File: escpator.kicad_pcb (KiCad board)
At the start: 4 copper layers, 45.7 x 15 mm, 36 parts, among them J1 Conn_01x04_Pin, J2 Conn_02x05_Odd_Even, J3 Conn_01x05, U1 STM32F103CBTx, U3 SRV05-4, U4 MCP1700x-330xxTT, X1 8MHz(12pF)

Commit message: second
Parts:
- removed X1: 8MHz(12pF), Crystal:Crystal_HC49-U_Vertical
- added Y1: Crystal_GND24, Crystal:Crystal_SMD_3225-4Pin_3.2x2.5mm_HandSoldering, F.Cu at (116.5, 36.9)
- C10, C14, C15, C3, C4, C5, C6, C7, C8, C9, R2, R3, R4, U3: moved to F.Cu
- C11, F1, R20, R27: moved to B.Cu
- moved C9 21.3 mm to (113.7, 33.0), turned to 0 degrees
- moved C10 17.7 mm to (109.4, 38.9), turned to 90 degrees
- moved C4 17.4 mm to (120.4, 32.1), turned to 180 degrees
- moved C3 15.5 mm to (108.4, 42.7), turned to -90 degrees
- moved R20 14.3 mm to (123.1, 40.5), turned to 90 degrees
- moved R1 13.5 mm to (123.5, 31.0)
- moved C5 12.9 mm to (120.4, 33.6), turned to 180 degrees
- moved R14 10.9 mm to (113.1, 38.8), turned to 135 degrees
- moved U4 10.7 mm to (133.2, 35.3), turned to -90 degrees
- moved C6 10.0 mm to (130.3, 33.0)
- moved C8 8.72 mm to (119.8, 40.4), turned to -90 degrees
- moved D1 5.74 mm to (111.3, 41.3), turned to 180 degrees
- moved R13 5.58 mm to (114.0, 31.3)
- moved R27 5.33 mm to (114.6, 42.3)
- moved D2 5.03 mm to (111.3, 42.8)
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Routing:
- net Earth: track 150.7 -> 195.2 mm, vias 13 -> 8
- net /AIN1: track 21.7 -> 4.45 mm, vias 2 -> 1
- net Net-(J2-Pin_3): track 20.5 -> 5.41 mm, vias 1 -> 0
- net /T_NRST: track 18.7 -> 3.91 mm
- net /T_JTMS: track 33.1 -> 20.7 mm, vias 4 -> 2
- net Net-(J2-Pin_2): track 25.6 -> 14.1 mm
- net /STLINK_TX: track 19.3 -> 26.6 mm
- net /LED_STLINK: track 14.7 -> 20.6 mm, vias 2 -> 1
- net Net-(J2-Pin_1): track 12.2 -> 17.9 mm, vias 1 -> 0
- net /T_JTCK: track 15.4 -> 20.5 mm
- net Net-(J1-Pin_1): track 12.8 -> 8.13 mm, vias 0 -> 1
- net /USB_P: track 11.5 -> 7.57 mm, vias 1 -> 0
- net +3V3: track 103.4 -> 99.5 mm, vias 7 -> 8
- net /OSC_OUT: track 10.8 -> 6.93 mm
- net /SWCLK: track 8.73 -> 5.13 mm
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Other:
- outline, holes or cut-outs redrawn

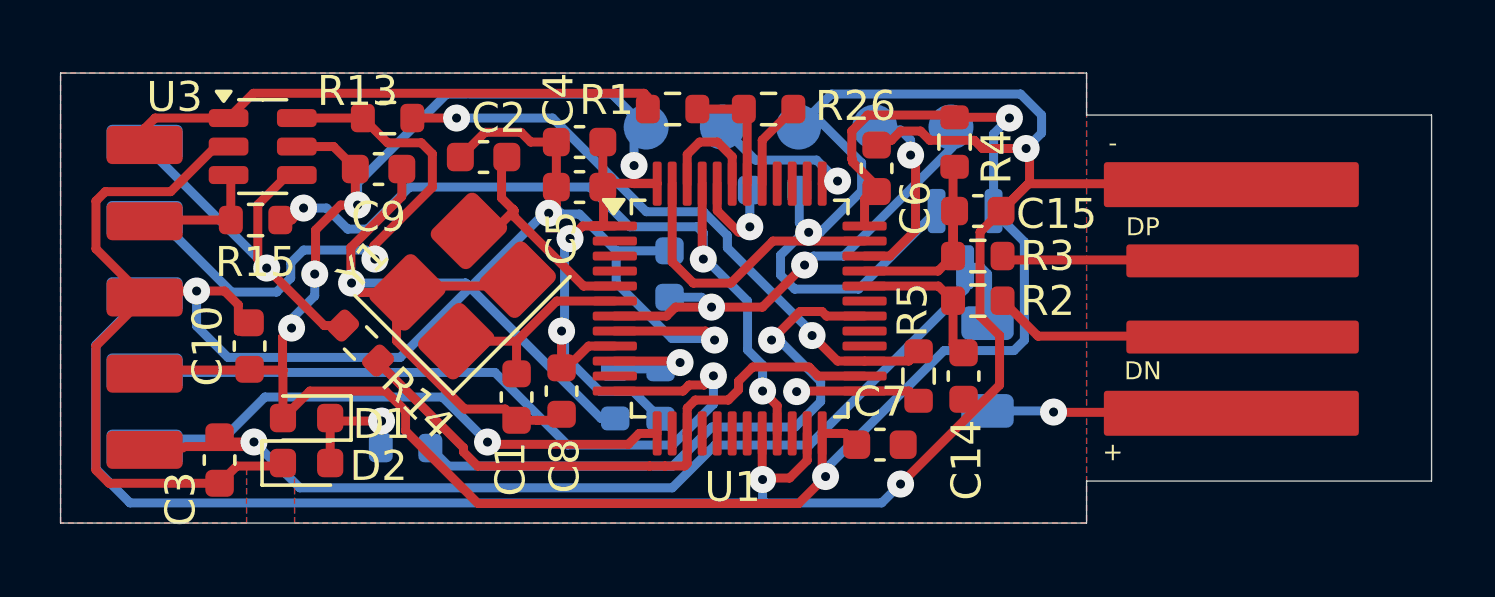
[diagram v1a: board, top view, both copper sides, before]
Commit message: presun LED plus otoceni USB
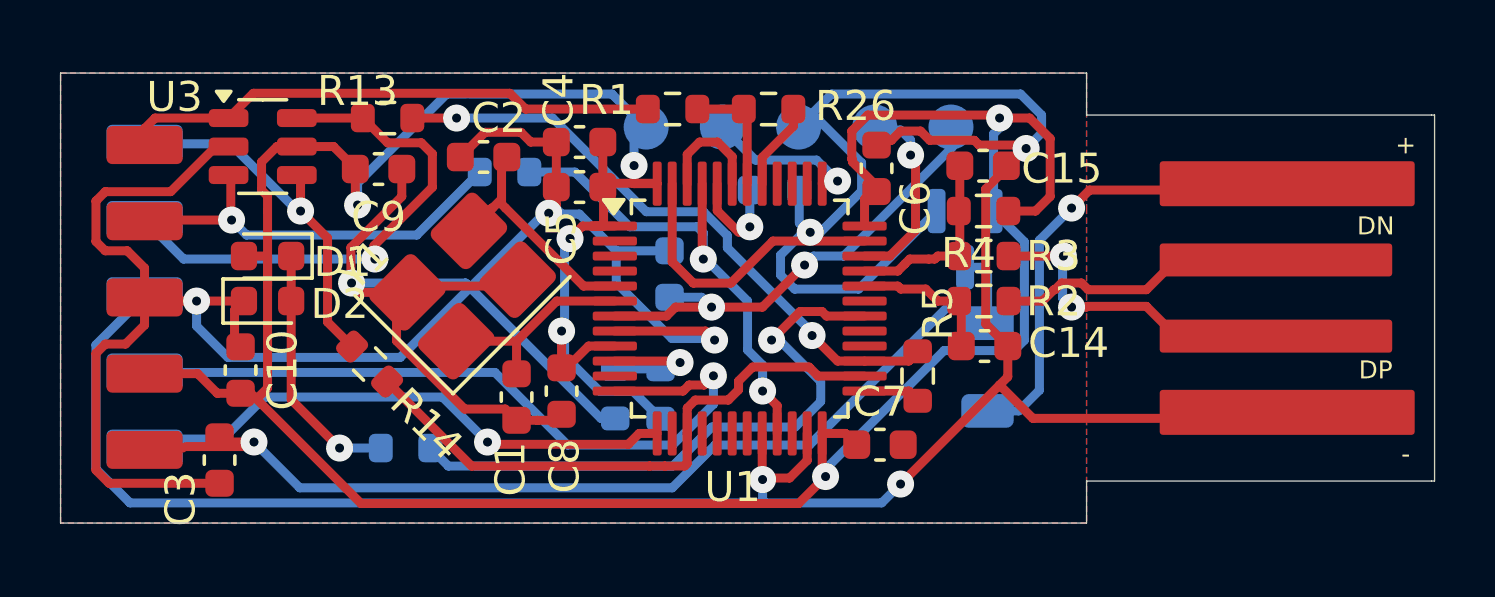
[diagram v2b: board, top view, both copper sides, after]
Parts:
- R15: moved to B.Cu
- moved J1 11.6 mm to (148.8, 37.3), turned to 180 degrees
- moved R15 8.45 mm to (117.9, 33.1)
- moved D1 5.55 mm to (110.0, 35.9)
- moved D2 5.55 mm to (110.0, 37.4)
- moved R4 2.49 mm to (133.9, 34.4), turned to 180 degrees
- moved C15 1.52 mm to (133.8, 32.9)
- moved C14 1.22 mm to (133.9, 38.9), turned to 0 degrees
- moved C10 0.85 mm to (109.1, 39.7)
- moved R14 0.76 mm to (113.4, 39.5)
- moved R2 0.20 mm to (133.9, 37.4)
- moved R3 0.20 mm to (133.9, 35.9)
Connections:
- net Net-(J1-Pin_2) renamed /D-
- net Net-(J1-Pin_3) renamed /D+
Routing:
- net Net-(J2-Pin_3): track 5.41 -> 14.8 mm, vias 0 -> 1
- net /T_SWIM: track 26.2 -> 17.1 mm, vias 3 -> 2
- net Net-(J1-Pin_1): track 8.13 -> 16.0 mm
- net +3V3: track 99.5 -> 106.1 mm, vias 8 -> 6
- net Net-(D1-K): track 4.48 -> 8.44 mm
- net /D+: track 8.04 -> 10.9 mm, vias 0 -> 2
- net /T_SWDIO_IN: track 4.41 -> 2.13 mm, vias 1 -> 0
- net /USB_P: track 7.57 -> 6.38 mm
- net /D-: track 8.48 -> 9.67 mm
- net Net-(J2-Pin_4): track 20.5 -> 19.4 mm
- net /T_JTCK: track 20.5 -> 19.8 mm
- net Net-(J2-Pin_2): track 14.1 -> 13.5 mm
- net /OSC_IN?: track 8.35 -> 8.90 mm
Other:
- board size 45.7 x 15 mm -> 45.8 x 15 mm

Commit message: changes
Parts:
- moved C3 1.10 mm to (109.5, 42.7)
- moved U4 0.90 mm to (134.2, 35.3)
- moved J3 0.88 mm to (126.7, 34.1)
- moved C6 0.81 mm to (129.8, 32.3)
- moved R26 0.48 mm to (126.5, 31.4)
- moved R1 0.27 mm to (123.5, 31.3)
- moved R7 0.07 mm to (126.8, 33.8)
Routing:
- net Earth: track 195.2 -> 181.7 mm
- net +3V3: track 106.1 -> 99.4 mm
- net +5V: track 36.1 -> 33.0 mm
- net /SWCLK: track 5.13 -> 7.12 mm
- net /T_SWIM: track 17.1 -> 15.9 mm
- net /SWDIO: track 6.55 -> 7.22 mm
- net /STM_RST: track 15.1 -> 15.7 mm
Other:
- board size 45.8 x 15 mm -> 45.7 x 15 mm
- board text added: "3V3"
- board text added: "5V"
- board text added: "STM_RST"
- board text added: "SWCLK"
- board text added: "SWDIO"
- board text added: "⏚"

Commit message: changedpins
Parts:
- removed U3: SRV05-4, Package_TO_SOT_SMD:SOT-23-6
- added R6: 100R, Resistor_SMD:R_0603_1608Metric, B.Cu at (32.2, 40.5)
- added R8: 100R, Resistor_SMD:R_0603_1608Metric, B.Cu at (30.7, 42.1)
- moved R14 79.7 mm to (33.7, 40.4)
- moved C7 78.7 mm to (51.7, 42.0)
- moved C1 78.7 mm to (39.6, 40.4)
- moved C11 78.7 mm to (44.7, 36.3)
- moved C14 78.7 mm to (55.2, 38.7)
- moved C15 78.7 mm to (55.2, 32.7)
- moved C2 78.7 mm to (38.5, 32.4)
- moved C3 78.7 mm to (30.8, 42.5)
- moved C4 78.7 mm to (41.7, 31.9)
- moved C5 78.7 mm to (41.7, 33.4)
- moved C6 78.7 mm to (51.2, 32.1)
- moved C8 78.7 mm to (41.1, 40.2)
- moved C9 78.7 mm to (35.0, 32.8)
- moved D1 78.7 mm to (31.3, 35.7)
- moved D2 78.7 mm to (31.3, 37.2)
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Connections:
- J2 pad 1: Net-(J2-Pin_1) -> +3V3
- J2 pad 10: /STLINK_RX -> Net-(J2-Pin_10)
- J2 pad 7: +3V3 -> Net-(J2-Pin_7)
- J2 pad 8: /STLINK_TX -> Net-(J2-Pin_8)
- R1 pad 1: Net-(J2-Pin_1) -> Net-(J2-Pin_7)
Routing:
- net Net-(J2-Pin_7): track 0.00 -> 32.7 mm, vias 0 -> 2
- net Net-(J2-Pin_1): track 18.1 -> 0.00 mm
- net /STLINK_TX: track 26.6 -> 18.6 mm
- net Earth: track 181.7 -> 174.5 mm, vias 8 -> 9
- net Net-(J2-Pin_8): track 0.00 -> 4.71 mm
- net /STLINK_RX: track 18.6 -> 15.0 mm
- net Net-(J2-Pin_10): track 0.00 -> 2.64 mm
- net Net-(J2-Pin_4): track 19.4 -> 16.9 mm
- net /LED_STLINK: track 20.6 -> 18.8 mm
- net Net-(J2-Pin_3): track 14.8 -> 13.2 mm
- net /T_JTCK: track 19.8 -> 20.8 mm
- net Net-(J2-Pin_2): track 13.5 -> 12.9 mm
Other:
- board text added: "GND"
- board text added: "RST"
- board text added: "RX"
- board text added: "SWIM"
- board text added: "TX"

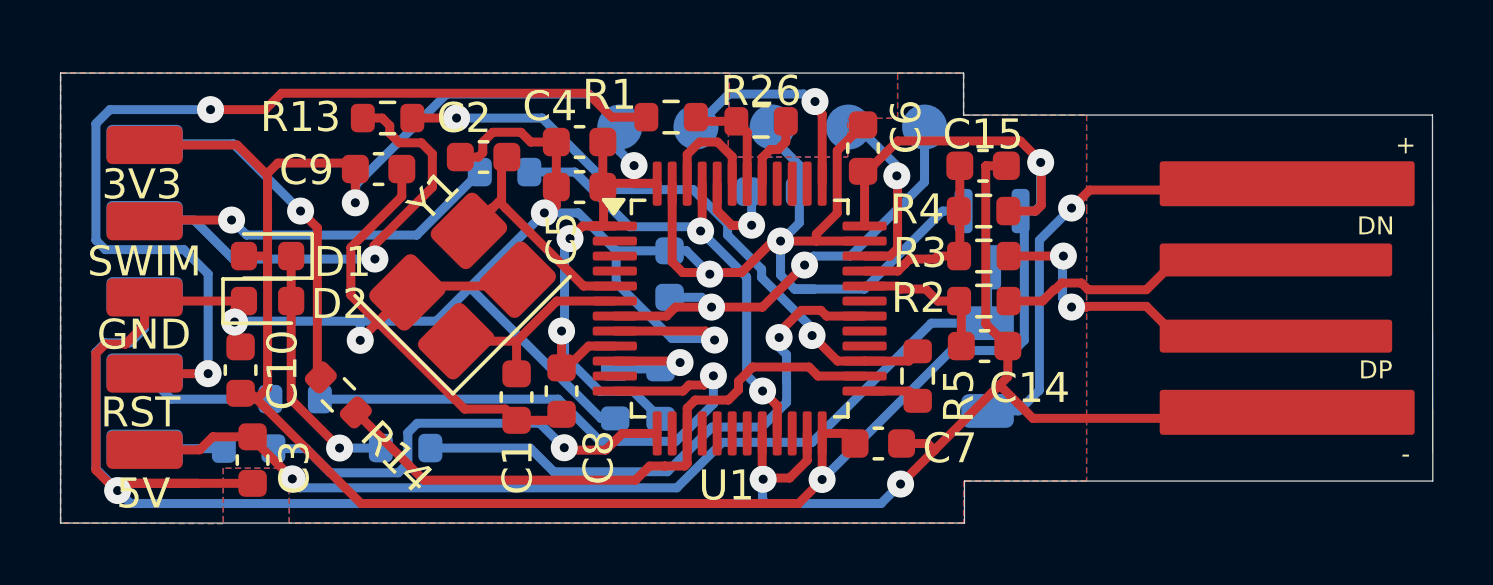
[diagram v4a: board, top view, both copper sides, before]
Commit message: flipped USB connector
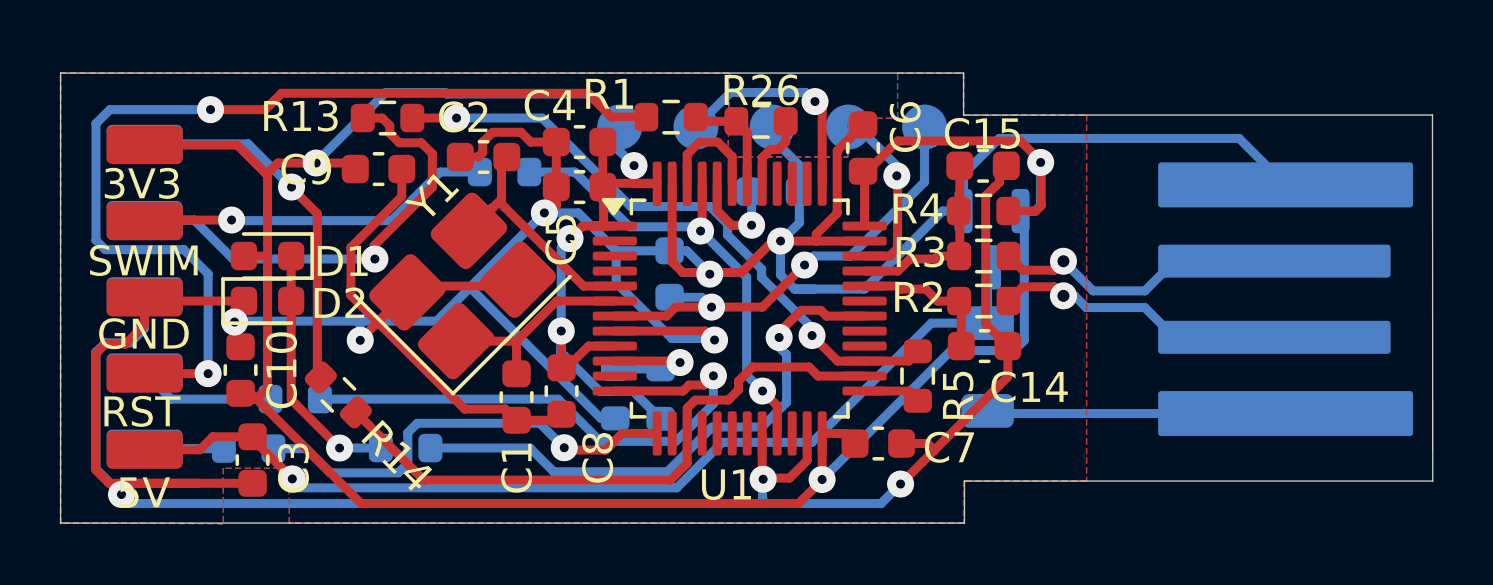
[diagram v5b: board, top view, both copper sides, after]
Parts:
- J1: moved to B.Cu
- moved J1 0.07 mm to (70.1, 37.2)
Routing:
- net Net-(J1-Pin_1): track 16.0 -> 9.97 mm, vias 1 -> 0
- net Earth: track 174.5 -> 177.2 mm
- net /D+: track 10.9 -> 10.0 mm, vias 2 -> 1
- net /D-: track 9.67 -> 9.75 mm, vias 0 -> 1
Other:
- board text removed: "⏚"

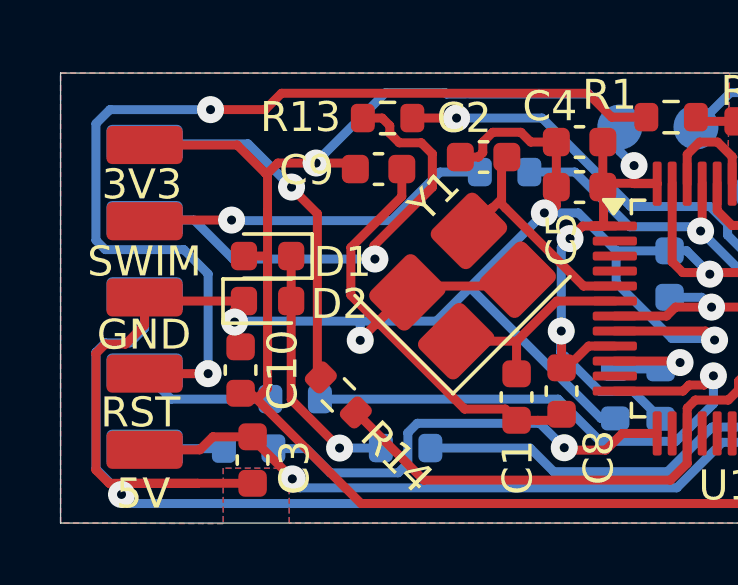
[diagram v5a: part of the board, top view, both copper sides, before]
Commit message: flip LED
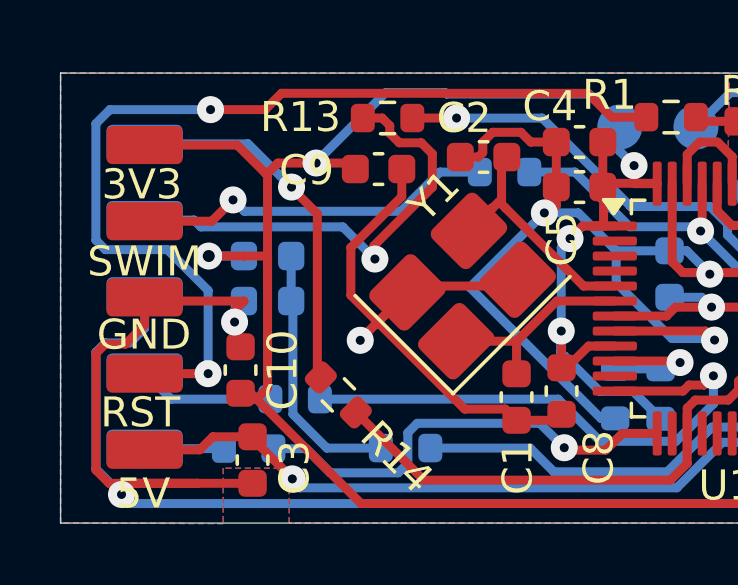
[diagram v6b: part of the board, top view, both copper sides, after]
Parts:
- D1, D2: moved to B.Cu
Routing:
- net Earth: track 177.2 -> 168.3 mm
- net +3V3: track 99.1 -> 101.5 mm, vias 6 -> 7
- net Net-(J2-Pin_3): track 12.8 -> 12.2 mm
- net Net-(D1-K): track 8.44 -> 8.69 mm, vias 1 -> 0

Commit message: aaa
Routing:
- net Earth: track 168.3 -> 182.7 mm, vias 9 -> 10
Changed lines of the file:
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@@
+	)
+	(segment
+		(start 27.350761 37.230761)
+		(end 27.230761 37.110761)
+		(width 0.3)
+		(layer "F.Cu")
+		(net 2)
 	)
 	(segment
@@
 	)
 	(segment
+		(start 30.230761 37.880761)
+		(end 29.580761 37.230761)
+		(width 0.3)
+		(layer "F.Cu")
+		(net 2)
+	)
+	(segment
 		(start 55.595239 33.404761)
 		(end 55.586987 33.404761)
@@
 	)
 	(segment
+		(start 30.230761 38.755761)
+		(end 30.230761 37.880761)
+		(width 0.3)
+		(layer "F.Cu")
+		(net 2)
+	)
+	(segment
 		(start 49.620761 34.998727)
 		(end 50.319261 34.300227)
@@
 	)
 	(segment
-		(start 30.230761 37.543261)
-		(end 30.543261 37.230761)
-		(width 0.3)
-		(layer "F.Cu")
-		(net 2)
-	)
-	(segment
 		(start 40.930761 41.205761)
 		(end 41.130761 41.005761)
@@
 	)
 	(segment
+		(start 57.47 39.68)
+		(end 56.081522 39.68)
+		(width 0.3)
+		(layer "F.Cu")
+		(net 2)
+	)
+	(segment
 		(start 45.171247 36.280761)
 		(end 47.126501 36.280761)
@@
 	)
 	(segment
+		(start 56.081522 39.68)
+		(end 56.005761 39.755761)
+		(width 0.3)
+		(layer "F.Cu")
+		(net 2)
+	)
+	(segment
 		(start 40.556648 34.293352)
 		(end 40.712963 34.293352)
@@
 	)
 	(segment
-		(start 30.230761 38.755761)
-		(end 30.230761 37.543261)
-		(width 0.3)
-		(layer "F.Cu")
-		(net 2)
-	)
-	(segment
 		(start 39.630761 41.205761)
 		(end 39.255761 40.830761)
@@
 	)
 	(segment
-		(start 27.350761 37.230761)
-		(end 30.543261 37.230761)
-		(width 0.3)
-		(layer "F.Cu")
-		(net 2)
-	)
-	(segment
 		(start 49.620761 35.230761)
 		(end 49.620761 34.998727)
@@
 	)
 	(segment
+		(start 29.580761 37.230761)
+		(end 27.350761 37.230761)
+		(width 0.3)
+		(layer "F.Cu")
+		(net 2)
+	)
+	(segment
 		(start 26.462462 43.417538)
 		(end 26.574239 43.305761)
@@
 		(start 44.818261 35.927775)
 		(end 45.171247 36.280761)
-		(width 0.3)
-		(layer "F.Cu")
-		(net 2)
-	)
-	(segment
-		(start 27.230761 37.110761)
-		(end 27.350761 37.230761)
 		(width 0.3)
 		(layer "F.Cu")
@@
 	)
 	(via
+		(at 57.47 39.68)
+		(size 0.9)
+		(drill 0.4)
+		(layers "F.Cu" "B.Cu")
+		(net 2)
+	)
+	(via
 		(at 46.230761 38.530761)
 		(size 0.9)
@@
 	)
 	(segment
+		(start 57.059 35.571975)
+		(end 57.059 39.269)
+		(width 0.3)
+		(layer "B.Cu")
+		(net 2)
+	)
+	(segment
+		(start 30.543261 37.618261)
+		(end 30.230761 37.930761)
+		(width 0.3)
+		(layer "B.Cu")
+		(net 2)
+	)
+	(segment
 		(start 41.689434 34.293352)
 		(end 42.951843 35.555761)
@@
 	)
 	(segment
+		(start 30.543261 37.230761)
+		(end 30.543261 37.618261)
+		(width 0.3)
+		(layer "B.Cu")
+		(net 2)
+	)
+	(segment
+		(start 54.530761 33.493262)
+		(end 56.214262 31.809761)
+		(width 0.3)
+		(layer "B.Cu")
+		(net 2)
+	)
+	(segment
 		(start 48.150761 31.430761)
 		(end 48.150761 31.800761)
@@
 	)
 	(segment
+		(start 54.530761 34.230761)
+		(end 54.530761 33.493262)
+		(width 0.3)
+		(layer "B.Cu")
+		(net 2)
+	)
+	(segment
 		(start 25.609761 42.824837)
 		(end 25.609761 38.936685)
@@
 	)
 	(segment
+		(start 57.432547 31.809761)
+		(end 57.901761 32.278975)
+		(width 0.3)
+		(layer "B.Cu")
+		(net 2)
+	)
+	(segment
 		(start 42.918261 41.143261)
 		(end 42.443261 41.143261)
@@
 	)
 	(segment
+		(start 56.214262 31.809761)
+		(end 57.432547 31.809761)
+		(width 0.3)
+		(layer "B.Cu")
+		(net 2)
+	)
+	(segment
 		(start 48.429761 36.362547)
 		(end 48.898975 36.831761)
@@
 	)
 	(segment
+		(start 57.901761 32.278975)
+		(end 57.901761 34.729214)
+		(width 0.3)
+		(layer "B.Cu")
+		(net 2)
+	)
+	(segment
 		(start 46.071691 36.334434)
 		(end 46.071691 36.321691)
@@
 	)
 	(segment
+		(start 57.901761 34.729214)
+		(end 57.059 35.571975)
+		(width 0.3)
+		(layer "B.Cu")
+		(net 2)
+	)
+	(segment
 		(start 38.080761 36.769239)
 		(end 38.080761 36.780761)
@@
 		(width 0.3)
 		(layer "B.Cu")
+		(net 2)
+	)
+	(segment
+		(start 57.059 39.269)
+		(end 57.47 39.68)
+		(width 0.3)
+		(layer "B.Cu")

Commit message: aaaaa
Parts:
- C3: moved to B.Cu
- moved C3 19.6 mm to (50.3, 40.5)
- moved R24 1.15 mm to (42.1, 39.5), turned to 0 degrees
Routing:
- net Earth: track 182.7 -> 165.4 mm, vias 10 -> 9
